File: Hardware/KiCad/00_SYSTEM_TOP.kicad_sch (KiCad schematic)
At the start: 0 parts

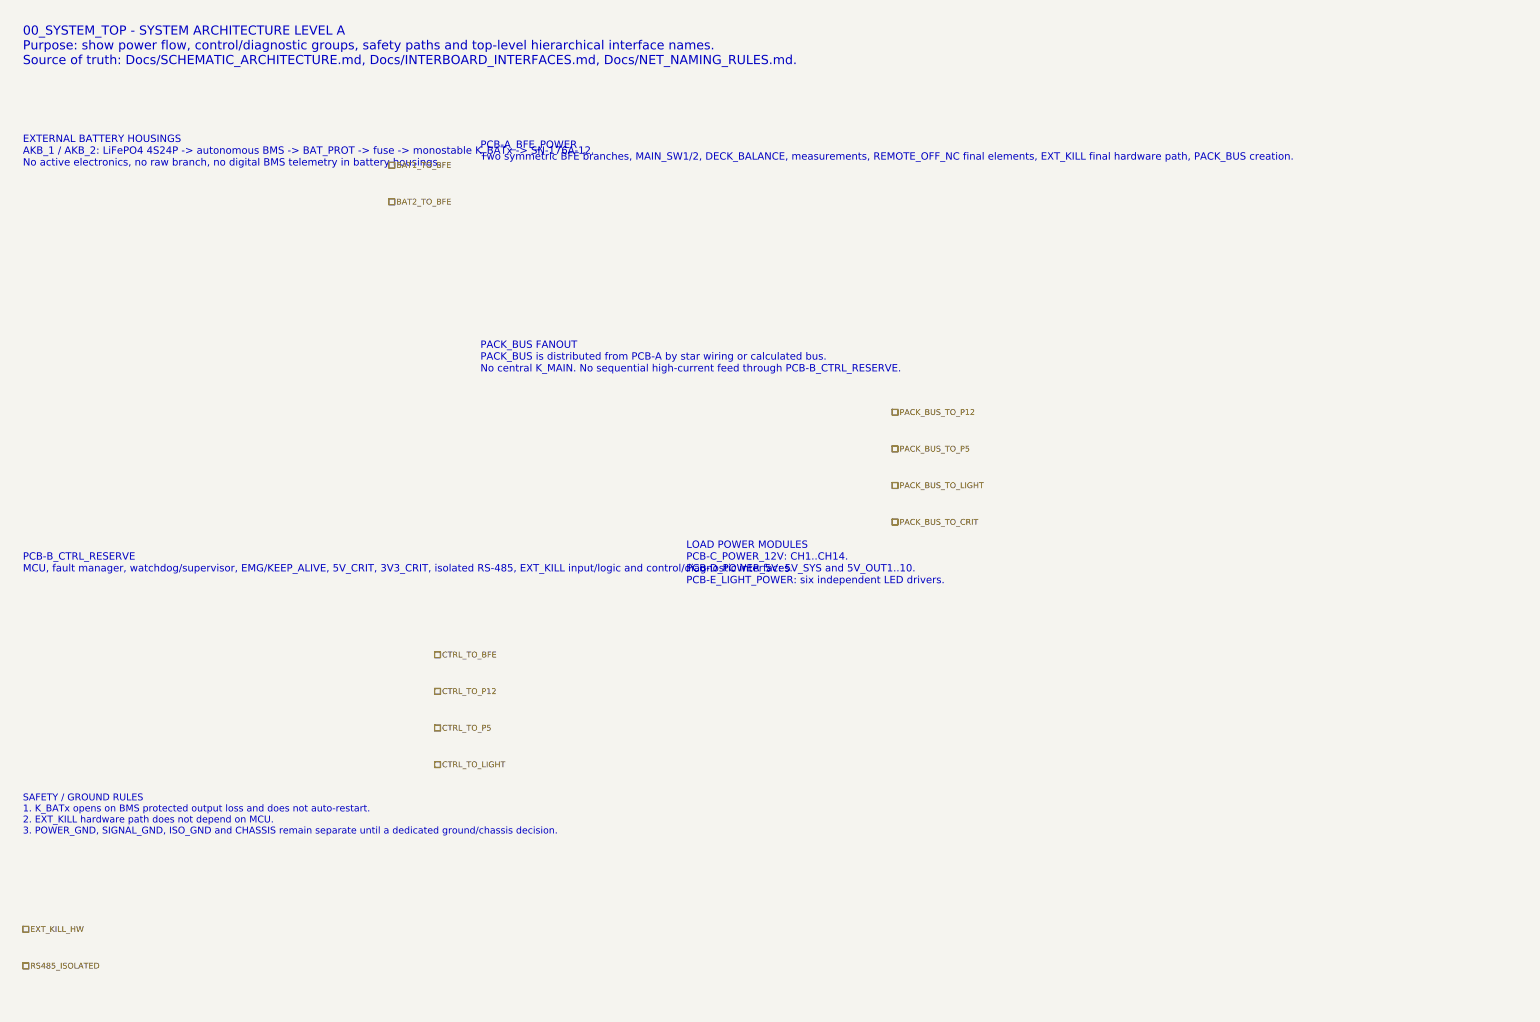
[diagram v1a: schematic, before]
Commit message: fix: improve 00_SYSTEM_TOP sheet layout readability
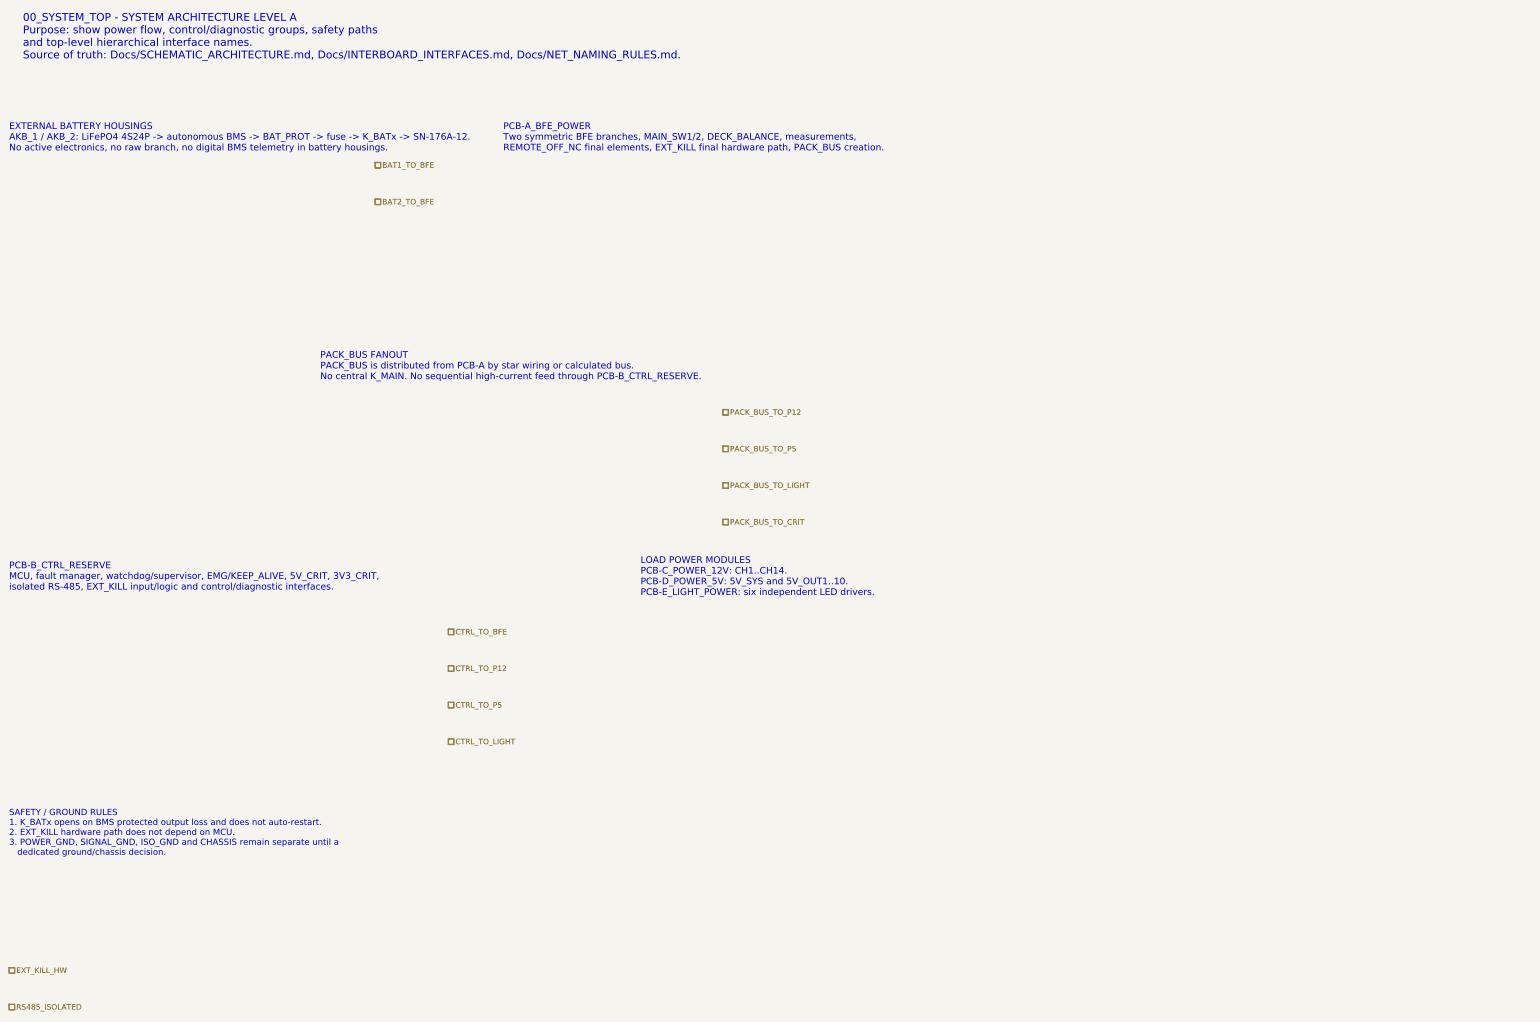
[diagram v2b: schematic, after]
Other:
- note added: "EXTERNAL BATTERY HOUSINGS AKB_1 / AKB_2: LiFePO4 4S24P -> autonomous BMS -> BAT_PROT -> fuse -> K_BATx -> SN-176A-12. No active electronics, no raw branch, no digital BMS telemetry in battery housings."
- note removed: "EXTERNAL BATTERY HOUSINGS AKB_1 / AKB_2: LiFePO4 4S24P -> autonomous BMS -> BAT_PROT -> fuse -> monostable K_BATx -> SN-176A-12. No active electronics, no raw branch, no digital BMS telemetry in battery housings."
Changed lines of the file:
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@@
 		(title "00_SYSTEM_TOP - PlataVM system overview")
 		(date "2026-07-15")
-		(rev "A1")
+		(rev "A2")
 		(company "Gonoboben/plataVM")
 		(comment 1 "Architecture Level A: functional blocks and hierarchical labels")
 		(comment 2 "No part numbers, footprints or PCB layout selected on this sheet")
 	)
-	(text "00_SYSTEM_TOP - SYSTEM ARCHITECTURE LEVEL A\nPurpose: show power flow, control/diagnostic groups, safety paths and top-level hierarchical interface names.\nSource of truth: Docs/SCHEMATIC_ARCHITECTURE.md, Docs/INTERBOARD_INTERFACES.md, Docs/NET_NAMING_RULES.md."
-		(exclude_from_sim no)
-		(at 15 12 0)
-		(effects
-			(font
-				(size 2 2)
-			)
-			(justify left)
-		)
-	)
-	(text "EXTERNAL BATTERY HOUSINGS\nAKB_1 / AKB_2: LiFePO4 4S24P -> autonomous BMS -> BAT_PROT -> fuse -> monostable K_BATx -> SN-176A-12.\nNo active electronics, no raw branch, no digital BMS telemetry in battery housings."
-		(exclude_from_sim no)
-		(at 15 35 0)
-		(effects
-			(font
-				(size 1.6 1.6)
-			)
-			(justify left)
-		)
-	)
-	(text "PCB-A_BFE_POWER\nTwo symmetric BFE branches, MAIN_SW1/2, DECK_BALANCE, measurements, REMOTE_OFF_NC final elements, EXT_KILL final hardware path, PACK_BUS creation."
-		(exclude_from_sim no)
-		(at 115 35 0)
-		(effects
-			(font
-				(size 1.6 1.6)
+	(text "00_SYSTEM_TOP - SYSTEM ARCHITECTURE LEVEL A\nPurpose: show power flow, control/diagnostic groups, safety paths\nand top-level hierarchical interface names.\nSource of truth: Docs/SCHEMATIC_ARCHITECTURE.md, Docs/INTERBOARD_INTERFACES.md, Docs/NET_NAMING_RULES.md."
+		(exclude_from_sim no)
+		(at 15 10 0)
+		(effects
+			(font
+				(size 1.7 1.7)
+			)
+			(justify left)
+		)
+	)
+	(text "EXTERNAL BATTERY HOUSINGS\nAKB_1 / AKB_2: LiFePO4 4S24P -> autonomous BMS -> BAT_PROT -> fuse -> K_BATx -> SN-176A-12.\nNo active electronics, no raw branch, no digital BMS telemetry in battery housings."
+		(exclude_from_sim no)
+		(at 12 32 0)
+		(effects
+			(font
+				(size 1.45 1.45)
+			)
+			(justify left)
+		)
+	)
+	(text "PCB-A_BFE_POWER\nTwo symmetric BFE branches, MAIN_SW1/2, DECK_BALANCE, measurements,\nREMOTE_OFF_NC final elements, EXT_KILL final hardware path, PACK_BUS creation."
+		(exclude_from_sim no)
+		(at 120 32 0)
+		(effects
+			(font
+				(size 1.45 1.45)
 			)
 			(justify left)
@@
 	(text "PACK_BUS FANOUT\nPACK_BUS is distributed from PCB-A by star wiring or calculated bus.\nNo central K_MAIN. No sequential high-current feed through PCB-B_CTRL_RESERVE."
 		(exclude_from_sim no)
-		(at 115 80 0)
-		(effects
-			(font
-				(size 1.6 1.6)
-			)
-			(justify left)
-		)
-	)
-	(text "PCB-B_CTRL_RESERVE\nMCU, fault manager, watchdog/supervisor, EMG/KEEP_ALIVE, 5V_CRIT, 3V3_CRIT, isolated RS-485, EXT_KILL input/logic and control/diagnostic interfaces."
-		(exclude_from_sim no)
-		(at 15 125 0)
-		(effects
-			(font
-				(size 1.6 1.6)
+		(at 80 82 0)
+		(effects
+			(font
+				(size 1.45 1.45)
+			)
+			(justify left)
+		)
+	)
+	(text "PCB-B_CTRL_RESERVE\nMCU, fault manager, watchdog/supervisor, EMG/KEEP_ALIVE, 5V_CRIT, 3V3_CRIT,\nisolated RS-485, EXT_KILL input/logic and control/diagnostic interfaces."
+		(exclude_from_sim no)
+		(at 12 128 0)
+		(effects
+			(font
+				(size 1.45 1.45)
 			)
 			(justify left)
@@
 	(text "LOAD POWER MODULES\nPCB-C_POWER_12V: CH1..CH14.\nPCB-D_POWER_5V: 5V_SYS and 5V_OUT1..10.\nPCB-E_LIGHT_POWER: six independent LED drivers."
 		(exclude_from_sim no)
-		(at 160 125 0)
-		(effects
-			(font
-				(size 1.6 1.6)
-			)
-			(justify left)
-		)
-	)
-	(text "SAFETY / GROUND RULES\n1. K_BATx opens on BMS protected output loss and does not auto-restart.\n2. EXT_KILL hardware path does not depend on MCU.\n3. POWER_GND, SIGNAL_GND, ISO_GND and CHASSIS remain separate until a dedicated ground/chassis decision."
-		(exclude_from_sim no)
-		(at 15 180 0)
-		(effects
-			(font
-				(size 1.5 1.5)
+		(at 150 128 0)
+		(effects
+			(font
+				(size 1.45 1.45)
+			)
+			(justify left)
+		)
+	)
+	(text "SAFETY / GROUND RULES\n1. K_BATx opens on BMS protected output loss and does not auto-restart.\n2. EXT_KILL hardware path does not depend on MCU.\n3. POWER_GND, SIGNAL_GND, ISO_GND and CHASSIS remain separate until a\n   dedicated ground/chassis decision."
+		(exclude_from_sim no)
+		(at 12 184 0)
+		(effects
+			(font
+				(size 1.35 1.35)
 			)
 			(justify left)
@@
 		(shape passive)
 		(exclude_from_sim no)
-		(at 95 38 0)
-		(effects
-			(font
-				(size 1.27 1.27)
+		(at 92 38 0)
+		(effects
+			(font
+				(size 1.2 1.2)
 			)
 			(justify left)
@@
 		(shape passive)
 		(exclude_from_sim no)
-		(at 95 46 0)
-		(effects
-			(font
-				(size 1.27 1.27)
+		(at 92 46 0)
+		(effects
+			(font
+				(size 1.2 1.2)
 			)
 			(justify left)
@@
 		(shape passive)
 		(exclude_from_sim no)
-		(at 205 92 0)
-		(effects
-			(font
-				(size 1.27 1.27)
+		(at 168 92 0)
+		(effects
+			(font
+				(size 1.2 1.2)
 			)
 			(justify left)
@@
 		(shape passive)
 		(exclude_from_sim no)
-		(at 205 100 0)
-		(effects
-			(font
-				(size 1.27 1.27)
+		(at 168 100 0)
+		(effects
+			(font
+				(size 1.2 1.2)
 			)
 			(justify left)
@@
 		(shape passive)
 		(exclude_from_sim no)
-		(at 205 108 0)
-		(effects
-			(font
-				(size 1.27 1.27)
+		(at 168 108 0)
+		(effects
+			(font
+				(size 1.2 1.2)
 			)
 			(justify left)
@@
 		(shape passive)
 		(exclude_from_sim no)
-		(at 205 116 0)
-		(effects
-			(font
-				(size 1.27 1.27)
+		(at 168 116 0)
+		(effects
+			(font
+				(size 1.2 1.2)
 			)
 			(justify left)
@@
 		(shape passive)
 		(exclude_from_sim no)
-		(at 105 145 0)
-		(effects
-			(font
-				(size 1.27 1.27)
+		(at 108 140 0)
+		(effects
+			(font
+				(size 1.2 1.2)
 			)
 			(justify left)
@@
 		(shape passive)
 		(exclude_from_sim no)
-		(at 105 153 0)
-		(effects
-			(font
-				(size 1.27 1.27)
+		(at 108 148 0)
+		(effects
+			(font
+				(size 1.2 1.2)
 			)
 			(justify left)
@@
 		(shape passive)
 		(exclude_from_sim no)
-		(at 105 161 0)
-		(effects
-			(font
-				(size 1.27 1.27)
+		(at 108 156 0)
+		(effects
+			(font
+				(size 1.2 1.2)
 			)
 			(justify left)
@@
 		(shape passive)
 		(exclude_from_sim no)
-		(at 105 169 0)
-		(effects
-			(font
-				(size 1.27 1.27)
+		(at 108 164 0)
+		(effects
+			(font
+				(size 1.2 1.2)
 			)
 			(justify left)
@@
 		(shape passive)
 		(exclude_from_sim no)
-		(at 15 205 0)
-		(effects
-			(font
-				(size 1.27 1.27)
+		(at 12 214 0)
+		(effects
+			(font
+				(size 1.2 1.2)
 			)
 			(justify left)
@@
 		(shape passive)
 		(exclude_from_sim no)
-		(at 15 213 0)
-		(effects
-			(font
-				(size 1.27 1.27)
-			)
-			(justify left)
+		(at 12 222 0)
+		(effects
+			(font
+				(size 1.2 1.2)
+			)
+			(justify left)
